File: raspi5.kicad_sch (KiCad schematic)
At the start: 6 parts, among them J1 GPIO, U1 FT24C256A

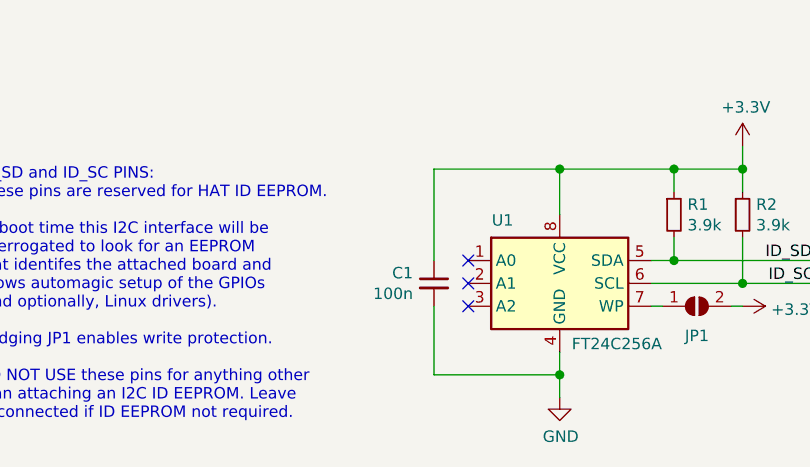
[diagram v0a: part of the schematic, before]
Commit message: Changed FPGA to new package and hooked up some more pins
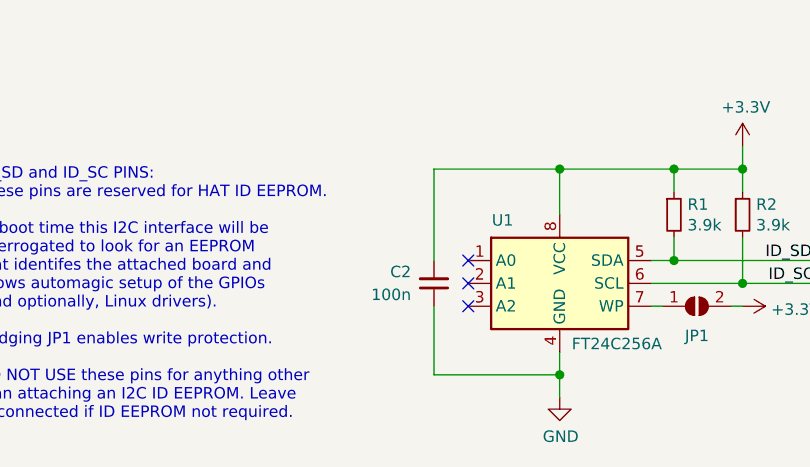
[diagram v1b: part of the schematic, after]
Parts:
- removed C1: 100n, symbol Device:C_Small
- added C2: 100n, Capacitor_SMD:C_0402_1005Metric_Pad0.74x0.62mm_HandSolder, symbol Device:C_Small
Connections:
- net +3V3: now also C2.2
- net GND: now also C2.1
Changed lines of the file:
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@@
     )
   )
-  (symbol (lib_id "Device:C_Small") (at 66.04 178.435 0) (unit 1)
-    (in_bom yes) (on_board yes) (dnp no)
-    (property "Reference" "C1" (at 63.7158 177.2856 0)
-      (effects (font (size 1.27 1.27)) (justify right))
+  (symbol (lib_id "Device:C_Small") (at 66.04 178.435 180) (unit 1)
+    (in_bom yes) (on_board yes) (dnp no) (fields_autoplaced)
+    (property "Reference" "C2" (at 63.5 177.1586 0)
+      (effects (font (size 1.27 1.27)) (justify left))
     )
-    (property "Value" "100n" (at 63.7158 179.5843 0)
-      (effects (font (size 1.27 1.27)) (justify right))
+    (property "Value" "100n" (at 63.5 179.6986 0)
+      (effects (font (size 1.27 1.27)) (justify left))
     )
-    (property "Footprint" "" (at 66.04 178.435 0)
+    (property "Footprint" "Capacitor_SMD:C_0402_1005Metric_Pad0.74x0.62mm_HandSolder" (at 66.04 178.435 0)
       (effects (font (size 1.27 1.27)) hide)
     )
-    (property "Datasheet" "~" (at 66.04 178.435 0)
+    (property "Datasheet" "https://datasheet.lcsc.com/lcsc/2304140030_Samsung-Electro-Mechanics-CL05B104KO5NNNC_C1525.pdf" (at 66.04 178.435 0)
       (effects (font (size 1.27 1.27)) hide)
     )
+    (property "LCSC" "C1525" (at 66.04 178.435 90)
+      (effects (font (size 1.27 1.27)) hide)
+    )
+    (pin "2")
     (pin "1")
-    (pin "2")
     (instances
       (project "Pi5-Artix50T-Hat"
-        (path "/e63e39d7-6ac0-4ffd-8aa3-1841a4541b55"
-          (reference "C1") (unit 1)
+        (path "/e63e39d7-6ac0-4ffd-8aa3-1841a4541b55/58f29d61-b732-4149-afb6-3ea37966fd1b/9687875a-5c78-4c5f-9fe3-711f7f6d52bf"
+          (reference "C2") (unit 1)
         )
         (path "/e63e39d7-6ac0-4ffd-8aa3-1841a4541b55/e4e6ab59-9796-41c2-b6d2-f170b467d852"

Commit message: Schematic finished, starting layout
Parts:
- added J3: 68711614522, 68711614522, symbol fpc:68711614522
- added JP7: ID_WP, Jumper:SolderJumper-2_P1.3mm_Open_TrianglePad1.0x1.5mm, symbol Jumper:SolderJumper_2_Open
- JP1: footprint (none) -> Jumper:SolderJumper-2_P1.3mm_Open_TrianglePad1.0x1.5mm
- R1, R2: footprint Resistor_SMD:R_0603_1608Metric_Pad0.98x0.95mm_HandSolder -> Resistor_SMD:R_0402_1005Metric_Pad0.72x0.64mm_HandSolder; LCSC C23018 -> (none)
- U1: footprint (none) -> Package_SO:MSOP-8_3x3mm_P0.65mm
- renumbered C2 to C1
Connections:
- net +3V3: now also JP7.1 (A); no longer J1.1 (Pin_1), J1.17 (Pin_17)
- net +5V: now also J3.15, J3.16
- net GND: now also J3.11, J3.14, J3.5, J3.8, J3.MP1, J3.MP2
- net GPIO10/SPI0.MOSI renamed SPI0_MOSI
- net GPIO11/SPI0.SCLK renamed SPI0_SCK
- net GPIO12/PWM0 renamed PI_GPIO12
- net GPIO13/PWM1 renamed PI_GPIO13
- net GPIO14/TXD0 renamed PI_UART_TX
- net GPIO15/RXD0 renamed PI_UART_RX
- net GPIO16 renamed SPI1_CE2
- net GPIO17 renamed SPI1_CE1
- net GPIO18/PCM.CLK renamed SPI1_CE0
- net GPIO19/PCM.FS renamed SPI1_MISO
- net GPIO20/PCM.DIN renamed SPI1_MOSI
- net GPIO21/PCM.DOUT renamed SPI1_SCK
- net GPIO22 renamed PI_GPIO22
- net GPIO23 renamed PI_GPIO23
- net GPIO24 renamed PI_GPIO24
- net GPIO25 renamed PI_GPIO25
- net GPIO26 renamed PI_GPIO26
- net GPIO27 renamed PI_GPIO27
- net GPIO2/SDA1 renamed PWR_SDA
- net GPIO3/SCL1 renamed PWR_SCL
- net GPIO4/GPCLK0 renamed PI_GPIO4
- net GPIO5 renamed PI_GPIO5
- net GPIO6 renamed PI_GPIO6
- net GPIO7/SPI0.CE1 renamed SPI0_CE1
- net GPIO8/SPI0.CE0 renamed SPI0_CE0
- net GPIO9/SPI0.MISO renamed SPI0_MISO
- new net: J1.1 (Pin_1), J1.17 (Pin_17), JP7.2 (B)
- new net PCIE_CLKN: J3.12
- new net PCIE_CLKP: J3.13
- new net PCIE_CLKREQ_N: J3.2
- new net PCIE_DET_WAKE: J3.3
- new net PCIE_PWR_EN: J3.4
- new net PCIE_RST_B: J3.1
- new net PCIE_RX0N: J3.9
- new net PCIE_RX0P: J3.10
- new net PCIE_TX0N: J3.6
- new net PCIE_TX0P: J3.7
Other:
- note added: "Datasheet: https://datasheets.raspberrypi.com/pcie/pcie-connector-standard.pdf"
- note added: "Details: https://github.com/raspberrypi/hats"
- note added: "GPIO Header"
- note added: "HAT EEPROM"
- note added: "I2C1"
- note added: "PCIe Header"
- note added: "Pi -> FPGA"
- note added: "Pi <- FPGA"
- note added: "Pi5 FPC 5V 1A max"
- note added: "Pinout notes: https://pinout.xyz/"
- note added: "The recommended FFC length is less than 50mm."
- note added: "Use our reg 3.3V"
- note added: "[GPIO]"
- note added: "[USBC]"
- note removed: "ADD PCIE CONNECTOR"
- title: Raspberry Pi 5 Connections -> FPGA Power
- moved on the sheet: C1, J1, JP1, R1, R2, U1

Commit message: Updated titleblock texts
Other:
- title: FPGA Power -> Raspberry Pi 5 - GPIO & PCIe Headers
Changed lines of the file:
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@@
   (paper "A4")
   (title_block
-    (title "FPGA Power")
-    (date "2024-02-11")
+    (title "Raspberry Pi 5 - GPIO & PCIe Headers")
+    (date "2024-02-14")
     (rev "0.1")
     (company "George Smart, M1GEO")

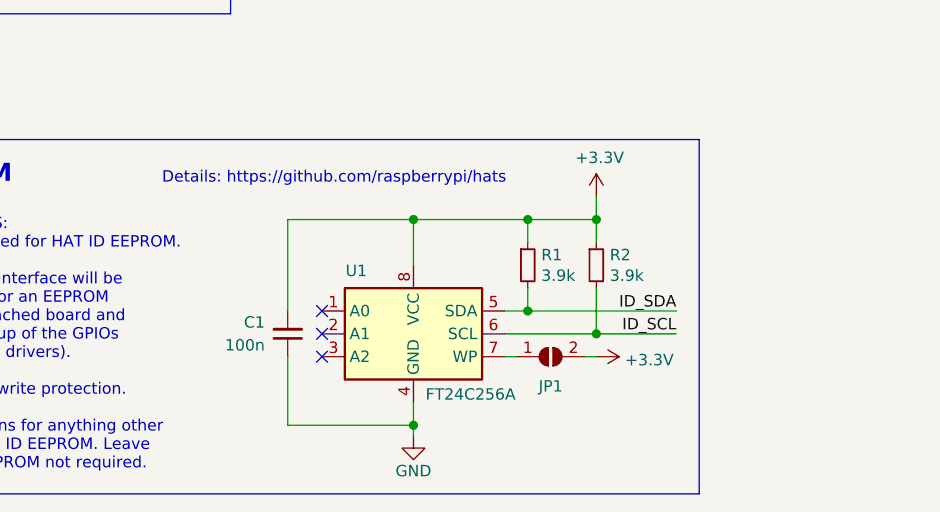
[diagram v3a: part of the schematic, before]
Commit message: Changed linear PSU for SMPS and a few other changes
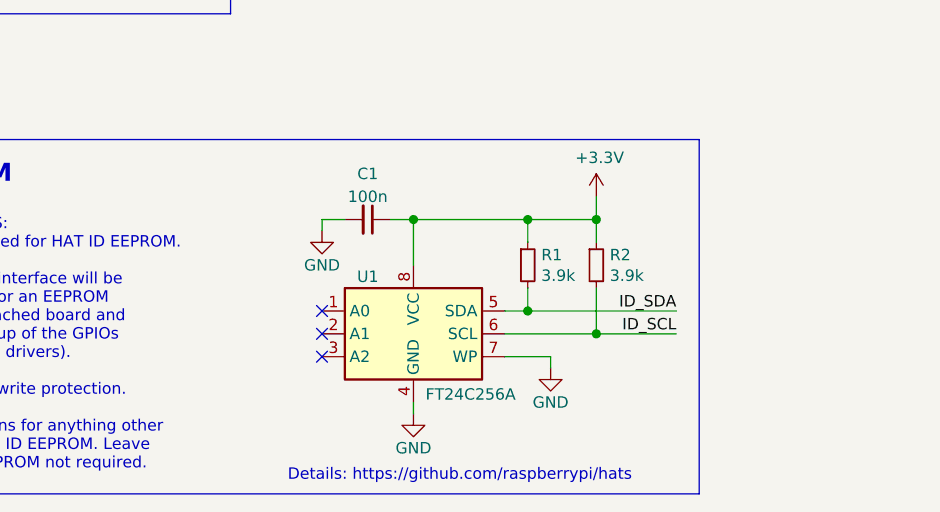
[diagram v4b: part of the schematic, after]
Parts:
- removed JP1: ID_WP, Jumper:SolderJumper-2_P1.3mm_Open_TrianglePad1.0x1.5mm, symbol Jumper:SolderJumper_2_Open
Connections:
- net +3V3: now also C1.1; no longer C1.2
- net GND: now also C1.2, U1.7 (WP); no longer C1.1
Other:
- moved on the sheet: C1
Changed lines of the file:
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@@
   (junction (at 87.63 72.39) (diameter 1.016) (color 0 0 0 0)
-  )
-  (junction (at 163.83 143.51) (diameter 1.016) (color 0 0 0 0)
   )
   (junction (at 186.69 76.2) (diameter 0) (color 0 0 0 0)
@@
     (stroke (width 0) (type solid))
   )
-  (wire (pts (xy 149.86 143.51) (xy 163.83 143.51))
-    (stroke (width 0) (type solid))
-  )
   (wire (pts (xy 105.41 57.15) (xy 102.87 57.15))
     (stroke (width 0) (type solid))
@@
     (stroke (width 0) (type default))
   )
-  (wire (pts (xy 173.99 135.89) (xy 175.26 135.89))
+  (wire (pts (xy 173.99 135.89) (xy 179.07 135.89))
     (stroke (width 0) (type solid))
   )
@@
     (stroke (width 0) (type solid))
   )
+  (wire (pts (xy 179.07 135.89) (xy 179.07 137.16))
+    (stroke (width 0) (type solid))
+  )
   (wire (pts (xy 76.2 38.1) (xy 74.93 38.1))
     (stroke (width 0) (type default))
@@
     (stroke (width 0) (type default))
   )
-  (wire (pts (xy 182.88 135.89) (xy 184.15 135.89))
-    (stroke (width 0) (type solid))
-  )
   (wire (pts (xy 105.41 77.47) (xy 105.41 82.55))
     (stroke (width 0) (type solid))
   )
+  (wire (pts (xy 156.21 120.65) (xy 153.67 120.65))
+    (stroke (width 0) (type solid))
+  )
   (wire (pts (xy 60.325 44.45) (xy 90.17 44.45))
     (stroke (width 0) (type solid))
@@
     (stroke (width 0) (type solid))
   )
+  (wire (pts (xy 153.67 120.65) (xy 153.67 121.92))
+    (stroke (width 0) (type default))
+  )
   (wire (pts (xy 102.87 62.23) (xy 129.54 62.23))
     (stroke (width 0) (type solid))
@@
     (stroke (width 0) (type default))
   )
-  (wire (pts (xy 163.83 143.51) (xy 163.83 144.78))
-    (stroke (width 0) (type solid))
-  )
   (wire (pts (xy 185.42 63.5) (xy 189.23 63.5))
     (stroke (width 0) (type default))
   )
+  (wire (pts (xy 163.83 140.97) (xy 163.83 142.24))
+    (stroke (width 0) (type solid))
+  )
   (wire (pts (xy 158.75 45.72) (xy 158.75 43.18))
     (stroke (width 0) (type default))
@@
     (stroke (width 0) (type default))
   )
-  (wire (pts (xy 149.86 135.89) (xy 149.86 143.51))
-    (stroke (width 0) (type solid))
-  )
-  (wire (pts (xy 149.86 120.65) (xy 149.86 130.81))
-    (stroke (width 0) (type solid))
-  )
   (wire (pts (xy 60.96 85.09) (xy 90.17 85.09))
     (stroke (width 0) (type solid))
   )
-  (wire (pts (xy 163.83 120.65) (xy 149.86 120.65))
+  (wire (pts (xy 163.83 120.65) (xy 161.29 120.65))
     (stroke (width 0) (type solid))
   )
@@
   (wire (pts (xy 185.42 50.8) (xy 189.23 50.8))
     (stroke (width 0) (type default))
-  )
-  (wire (pts (xy 163.83 140.97) (xy 163.83 143.51))
-    (stroke (width 0) (type solid))
   )
   (wire (pts (xy 185.42 48.26) (xy 189.23 48.26))
@@
     (effects (font (size 1.27 1.27)) (justify left bottom))
   )
-  (text "Details: https://github.com/raspberrypi/hats" (at 135.89 116.84 0)
+  (text "Details: https://github.com/raspberrypi/hats" (at 149.86 149.86 0)
     (effects (font (size 1.27 1.27)) (justify left bottom))
   )
@@
     )
   )
-  (symbol (lib_id "Device:C_Small") (at 149.86 133.35 180) (unit 1)
-    (in_bom yes) (on_board yes) (dnp no) (fields_autoplaced)
-    (property "Reference" "C1" (at 147.32 132.0736 0)
-      (effects (font (size 1.27 1.27)) (justify left))
-    )
-    (property "Value" "100n" (at 147.32 134.6136 0)
-      (effects (font (size 1.27 1.27)) (justify left))
-    )
-    (property "Footprint" "Capacitor_SMD:C_0402_1005Metric_Pad0.74x0.62mm_HandSolder" (at 149.86 133.35 0)
-      (effects (font (size 1.27 1.27)) hide)
-    )
-    (property "Datasheet" "https://datasheet.lcsc.com/lcsc/2304140030_Samsung-Electro-Mechanics-CL05B104KO5NNNC_C1525.pdf" (at 149.86 133.35 0)
-      (effects (font (size 1.27 1.27)) hide)
-    )
-    (property "LCSC" "C1525" (at 149.86 133.35 90)
+  (symbol (lib_id "Device:C_Small") (at 158.75 120.65 270) (unit 1)
+    (in_bom yes) (on_board yes) (dnp no)
+    (property "Reference" "C1" (at 158.75 115.57 90)
+      (effects (font (size 1.27 1.27)))
+    )
+    (property "Value" "100n" (at 158.75 118.11 90)
+      (effects (font (size 1.27 1.27)))
+    )
+    (property "Footprint" "Capacitor_SMD:C_0402_1005Metric_Pad0.74x0.62mm_HandSolder" (at 158.75 120.65 0)
+      (effects (font (size 1.27 1.27)) hide)
+    )
+    (property "Datasheet" "https://datasheet.lcsc.com/lcsc/2304140030_Samsung-Electro-Mechanics-CL05B104KO5NNNC_C1525.pdf" (at 158.75 120.65 0)
+      (effects (font (size 1.27 1.27)) hide)
+    )
+    (property "LCSC" "C1525" (at 158.75 120.65 90)
       (effects (font (size 1.27 1.27)) hide)
     )
@@
   (symbol (lib_id "Memory_EEPROM:CAT24C256") (at 163.83 133.35 0) (unit 1)
     (in_bom yes) (on_board yes) (dnp no)
-    (property "Reference" "U1" (at 157.48 126.3458 0)
+    (property "Reference" "U1" (at 158.75 127 0)
       (effects (font (size 1.27 1.27)))
     )
@@
     )
   )
-  (symbol (lib_id "power:GND") (at 163.83 144.78 0) (unit 1)
+  (symbol (lib_id "power:GND") (at 163.83 142.24 0) (unit 1)
     (in_bom yes) (on_board yes) (dnp no)
-    (property "Reference" "#PWR03" (at 163.83 151.13 0)
-      (effects (font (size 1.27 1.27)) hide)
-    )
-    (property "Value" "GND" (at 163.83 148.59 0)
-      (effects (font (size 1.27 1.27)))
-    )
-    (property "Footprint" "" (at 163.83 144.78 0)
-      (effects (font (size 1.27 1.27)))
-    )
-    (property "Datasheet" "" (at 163.83 144.78 0)
+    (property "Reference" "#PWR03" (at 163.83 148.59 0)
+      (effects (font (size 1.27 1.27)) hide)
+    )
+    (property "Value" "GND" (at 163.83 146.05 0)
+      (effects (font (size 1.27 1.27)))
+    )
+    (property "Footprint" "" (at 163.83 142.24 0)
+      (effects (font (size 1.27 1.27)))
+    )
+    (property "Datasheet" "" (at 163.83 142.24 0)
       (effects (font (size 1.27 1.27)))
     )
@@
     )
   )
-  (symbol (lib_id "Jumper:SolderJumper_2_Open") (at 179.07 135.89 0) (unit 1)
-    (in_bom yes) (on_board yes) (dnp no)
-    (property "Reference" "JP1" (at 179.07 139.173 0)
-      (effects (font (size 1.27 1.27)))
-    )
-    (property "Value" "ID_WP" (at 179.07 133.096 0)
-      (effects (font (size 1.27 1.27)) hide)
-    )
-    (property "Footprint" "Jumper:SolderJumper-2_P1.3mm_Open_TrianglePad1.0x1.5mm" (at 179.07 135.89 0)
-      (effects (font (size 1.27 1.27)) hide)
-    )
-    (property "Datasheet" "~" (at 179.07 135.89 0)
-      (effects (font (size 1.27 1.27)) hide)
-    )
-    (pin "1")
-    (pin "2")
-    (instances
-      (project "Pi5-Artix50T-Hat"
-        (path "/e63e39d7-6ac0-4ffd-8aa3-1841a4541b55/e4e6ab59-9796-41c2-b6d2-f170b467d852"
-          (reference "JP1") (unit 1)
-        )
-      )
-    )
-  )
   (symbol (lib_id "power:+5V") (at 105.41 38.1 0) (unit 1)
     (in_bom yes) (on_board yes) (dnp no)
@@
     )
   )
+  (symbol (lib_id "power:GND") (at 153.67 121.92 0) (unit 1)
+    (in_bom yes) (on_board yes) (dnp no)
+    (property "Reference" "#PWR046" (at 153.67 128.27 0)
+      (effects (font (size 1.27 1.27)) hide)
+    )
+    (property "Value" "GND" (at 153.67 125.73 0)
+      (effects (font (size 1.27 1.27)))
+    )
+    (property "Footprint" "" (at 153.67 121.92 0)
+      (effects (font (size 1.27 1.27)))
+    )
+    (property "Datasheet" "" (at 153.67 121.92 0)
+      (effects (font (size 1.27 1.27)))
+    )
+    (pin "1")
+    (instances
+      (project "Pi5-Artix50T-Hat"
+        (path "/e63e39d7-6ac0-4ffd-8aa3-1841a4541b55/e4e6ab59-9796-41c2-b6d2-f170b467d852"
+          (reference "#PWR046") (unit 1)
+        )
+      )
+    )
+  )
   (symbol (lib_id "power:PWR_FLAG") (at 108.585 39.37 0) (unit 1)
     (in_bom yes) (on_board yes) (dnp no)
@@
     )
   )
-  (symbol (lib_id "power:+3.3V") (at 184.15 135.89 270) (unit 1)
+  (symbol (lib_id "power:GND") (at 179.07 137.16 0) (unit 1)
     (in_bom yes) (on_board yes) (dnp no)
-    (property "Reference" "#PWR07" (at 180.34 135.89 0)
-      (effects (font (size 1.27 1.27)) hide)
-    )
-    (property "Value" "+3.3V" (at 187.3251 136.2583 90)
-      (effects (font (size 1.27 1.27)) (justify left))
-    )
-    (property "Footprint" "" (at 184.15 135.89 0)
-      (effects (font (size 1.27 1.27)) hide)
-    )
-    (property "Datasheet" "" (at 184.15 135.89 0)
-      (effects (font (size 1.27 1.27)) hide)
+    (property "Reference" "#PWR07" (at 179.07 143.51 0)
+      (effects (font (size 1.27 1.27)) hide)
+    )
+    (property "Value" "GND" (at 179.07 140.97 0)
+      (effects (font (size 1.27 1.27)))
+    )
+    (property "Footprint" "" (at 179.07 137.16 0)
+      (effects (font (size 1.27 1.27)))
+    )
+    (property "Datasheet" "" (at 179.07 137.16 0)
+      (effects (font (size 1.27 1.27)))
     )
     (pin "1")

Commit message: Started routing. More to go
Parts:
- removed JP7: ID_WP, Jumper:SolderJumper-2_P1.3mm_Open_TrianglePad1.0x1.5mm, symbol Jumper:SolderJumper_2_Open
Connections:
- net +3V3 is gone; now on net +3.3VP: C1.1, R1.1, R2.1, U1.8 (VCC)
- net GND: now also U1.1 (A0), U1.2 (A1), U1.3 (A2)
- net +3.3VP: now reaches J1.1 (Pin_1), J1.17 (Pin_17)
- net PWR_SCL renamed PI_GPIO3
- net PWR_SDA renamed PI_GPIO2
- net SPI0_CE0 renamed PI_GPIO8
- net SPI0_CE1 renamed PI_GPIO7
- net SPI1_CE0 renamed PI_GPIO18
- net SPI1_CE1 renamed PI_GPIO17
- net SPI1_CE2 renamed PI_GPIO16
- net SPI1_MISO renamed PI_GPIO19
- net SPI1_MOSI renamed PI_GPIO20
- net SPI1_SCK renamed PI_GPIO21_CC
- no-connect marks 3 -> 0
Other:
- note added: "EEPROM"
- note added: "Use Pi 3.3V"
- note removed: "I2C1"
- note removed: "Use our reg 3.3V"
